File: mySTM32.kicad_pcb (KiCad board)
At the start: 2 copper layers, 138 x 108 mm, 122 parts, among them J1 conn1X2, J10 DB9_Female****, J11 USB_OTG, J12 conn2X16, J13 conn2X3, J14 Conn_02x02, J15 conn2X3, J16 conn1X2, J17 conn2X2, J18 JTAG, J19 Conn_02x17_Odd_Even, J2 USB_OTG, J20 Conn_02x22_Odd_Even, J21 conn2X9, J22 conn2X3, J23 Conn2x4, J3 conn2X3, J4 conn2X2, J5 conn2X2, J6 conn1X2, J7 Conn_01x02, J8 Conn2x4, J9 conn2X4, Q1 Q_NPN_BEC(S8050), Q2 Q_NPN_BEC, Q3 Q_NPN_BEC(S8050), SW1 KFT8.0, SW2 WAKUP, SW3 RESET, SW4 KE1, SW5 KEY2, U1 AT24C02, U2 W25Q16, U3 SD-Card, U4 SP3485, U5 SN65HVD230, U6 CH340G, U7 AMS1117, U8 SP3232, U9 STM32F103VET6, Y1 12MHz, Y2 32.768KHz, Y3 8MHz

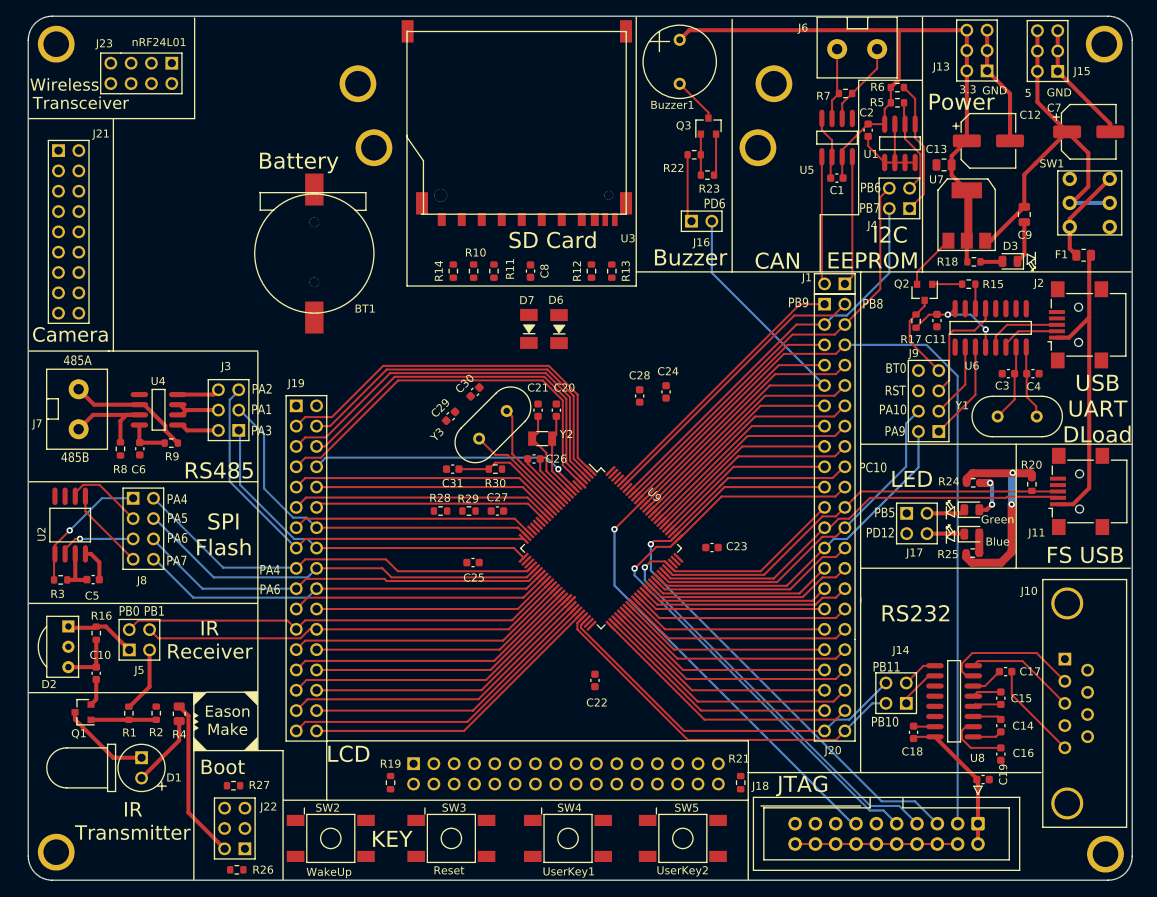
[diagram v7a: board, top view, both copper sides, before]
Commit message: [Battery] route, footprint pad [Decouple Cap]
Signed-off-by: EasonLiang <liangyx25@163.com>
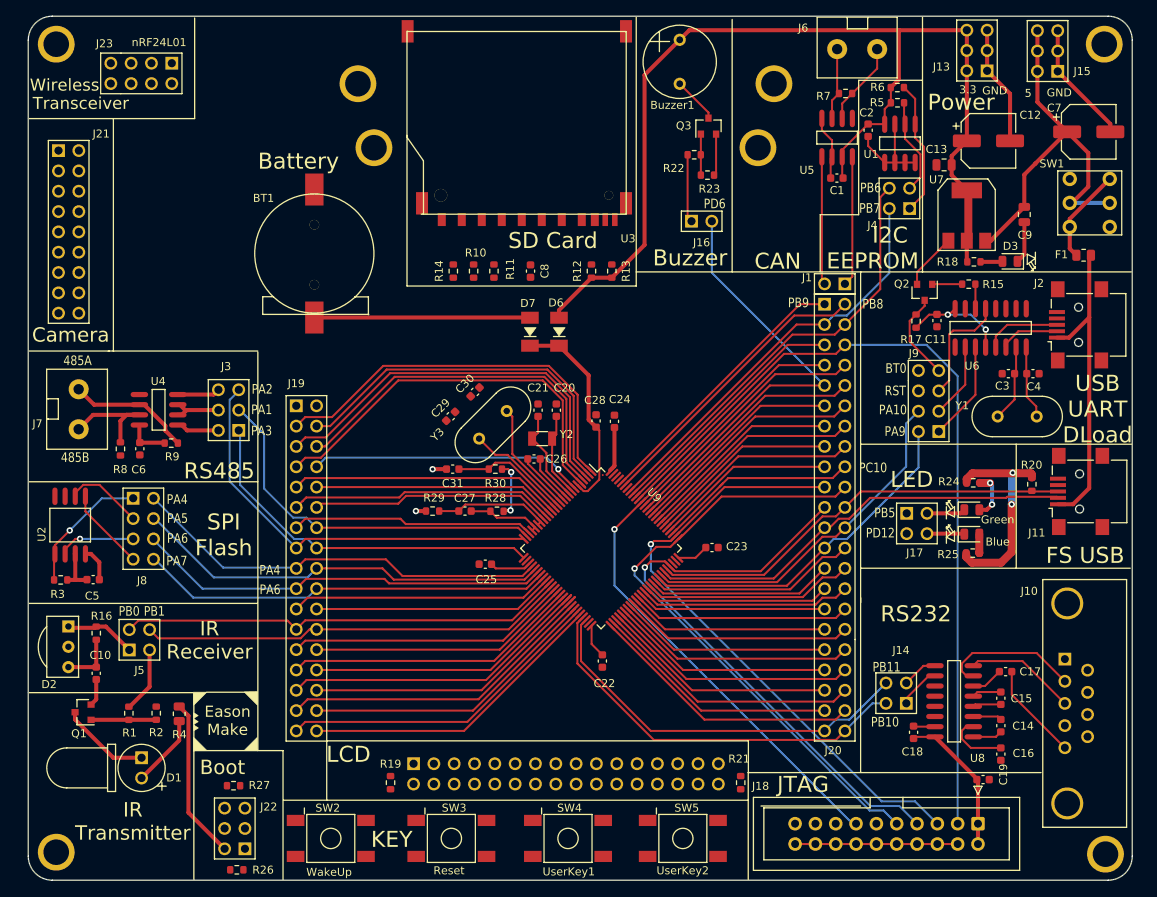
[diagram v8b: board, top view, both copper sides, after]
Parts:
- moved C24 7.43 mm to (103.3, 80.6)
- moved R28 7.06 mm to (88.6, 91.9), turned to 0 degrees
- moved C28 6.28 mm to (101.0, 80.6)
- moved R29 4.55 mm to (80.5, 91.9), turned to 180 degrees
- moved C27 4.05 mm to (84.6, 91.9)
- moved C22 2.60 mm to (101.8, 110.6)
- moved C25 1.55 mm to (87.1, 98.5)
- moved D7 0.38 mm to (92.7, 69.4)
- moved D6 0.33 mm to (96.3, 69.4)
- turned BT1 to 270 degrees
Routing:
- net +3V3: track 194.6 -> 262.6 mm, vias 4 -> 6
- net Net-(BT1-Pad1): track 0.00 -> 27.0 mm
- net Net-(C28-Pad2): track 0.00 -> 26.3 mm
- net GNDA: track 0.00 -> 14.4 mm
- net /V3.3V: track 0.00 -> 9.33 mm
- net GND: track 118.0 -> 121.3 mm, vias 0 -> 2
- net /PB10: track 48.0 -> 50.5 mm
- net /PB11: track 47.2 -> 49.6 mm
- net /OV_PC3: track 29.4 -> 30.2 mm
- net /OV_PC2: track 32.7 -> 33.3 mm
